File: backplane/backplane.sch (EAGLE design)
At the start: 18 parts, among them J1 09232486825, J2 09232486825, J3 09232486825, J4 09232486825, J5 09232486825, J6 09232486825, J7 09232486825, J8 09232486825, U1 LM1084IS-5.0, U2 LM1084IS-3.3, U3 ESP32-DEVKITC-32D

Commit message: modified backplane
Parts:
- removed C1, C3: 10Uf, rc-master-smd:CP_3216
- removed C2, C4: 10Uf, rc-master-smd:C_1206
- removed JP1: (no value), pinhead:PINHD-1X19
- removed JP2: (no value), pinhead:PINHD-2X15
- removed U1: LM1084IS-5.0, LM1084IS:LM1084IS-5.0
- removed U2: LM1084IS-3.3, LM1084IS:LM1084IS-3.3
- removed U3: ESP32-DEVKITC-32D, ESP32-DEVKITC-32D:ESP32-DEVKITC-32D
- removed XS1: (no value), polyvent_power_connector:CURTIS_INDUSTRIES_T38120-02-0
- added J9: TB009-508-04BE, TB009-508-04BE:TB009-508-04BE
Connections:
- removed net N$1: C3.+, U2.IN
- removed net N$2: C1.+, U1.IN
- removed net N$3: JP1.16, U3.TXD0
- removed net N$4: JP1.15, U3.RXD0
- removed net N$5: JP1.6, U3.IO0
- removed net N$6: JP1.5, U3.IO2
- removed net N$7: JP1.3, U3.SD1
- removed net N$8: JP1.2, U3.SD0
- removed net N$9: JP1.1, U3.CLK
- removed net VCC: U3.EXT_5V
- net 24V/12V: now also J9.2; no longer XS1.P$2
- net 3.3V: now also J1.A7, J1.B7, J2.A7, J2.B7, J3.A7, J3.B7, J4.A7, J4.B7, J5.A7, J5.B7, J6.A7, J6.B7, J7.A7, J7.B7, J8.A7, J8.B7, J9.4; no longer C4.2, J1.C6, J2.C6, J3.C6, J4.C6, J5.C6, J6.C6, J7.C6, J8.C6, JP2.5, U2.OUT, U2.VOUT, U3.3V3
- net 5V: now also J1.C6, J2.C6, J3.C6, J4.C6, J5.C6, J6.C6, J7.C6, J8.C6, J9.3; no longer C2.2, J1.A7, J1.B7, J2.A7, J2.B7, J3.A7, J3.B7, J4.A7, J4.B7, J5.A7, J5.B7, J6.A7, J6.B7, J7.A7, J7.B7, J8.A7, J8.B7, JP2.3, U1.OUT, U1.VOUT
- net EXT_1: no longer JP2.17
- net EXT_2: no longer JP2.19
- net EXT_3: no longer JP2.21
- net EXT_4: no longer JP2.23
- net EXT_5: no longer JP2.25
- net EXT_6: no longer JP2.27
- net EXT_7: no longer JP2.29
- net GND: now also J9.1; no longer C1.-, C2.1, C3.-, C4.1, JP1.13, JP1.19, JP2.1, U1.ADJ/GND, U2.ADJ/GND, U3.GND1, U3.GND2, U3.GND3, XS1.P$1
- net MISO: no longer JP1.12, JP2.9, U3.IO19
- net MOSI: no longer JP1.18, JP2.11, U3.IO23
- net SCK: no longer JP1.11, JP2.7, U3.IO18
- net SCL: no longer JP2.15
- net SDA: no longer JP2.13
- net SS_1: no longer JP1.7, JP2.30, U3.IO4
- net SS_10: no longer JP2.12, U3.IO25
- net SS_11: no longer JP2.10, U3.IO26
- net SS_12: no longer JP2.8, U3.IO32
- net SS_13: no longer JP2.6, U3.IO33
- net SS_14: no longer JP2.4
- net SS_15: no longer JP2.2
- net SS_2: no longer JP1.10, JP2.28, U3.IO5
- net SS_3: no longer JP2.26, U3.IO13
- net SS_4: no longer JP2.24, U3.IO14
- net SS_5: no longer JP1.4, JP2.22, U3.IO15
- net SS_6: no longer JP1.8, JP2.20, U3.IO16
- net SS_7: no longer JP1.9, JP2.18, U3.IO17
- net SS_8: no longer JP1.14, JP2.16, U3.IO21
- net SS_9: no longer JP1.17, JP2.14, U3.IO22

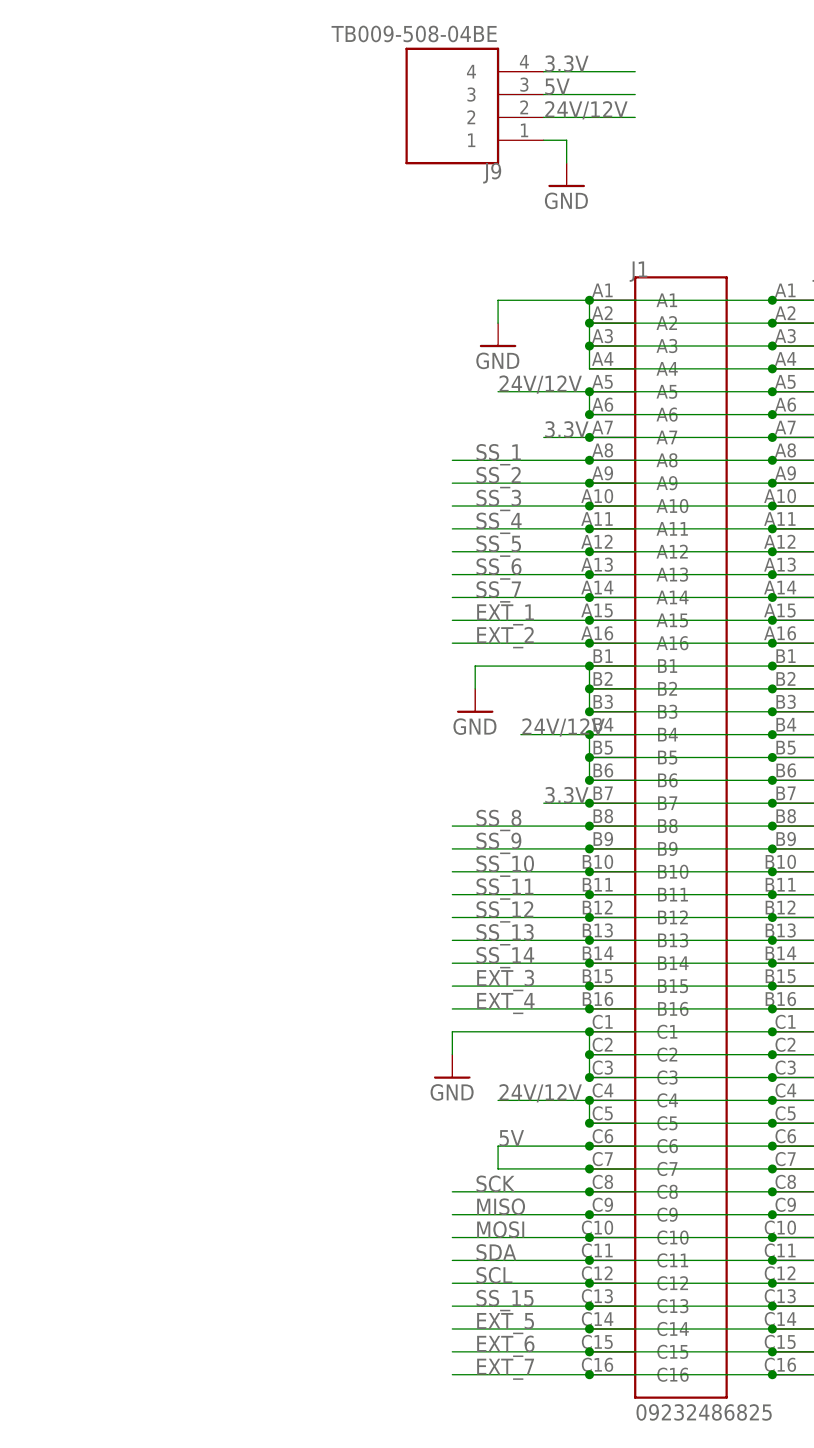
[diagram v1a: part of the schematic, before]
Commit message: added labeled backplane breakout connector, backplane pcb is done
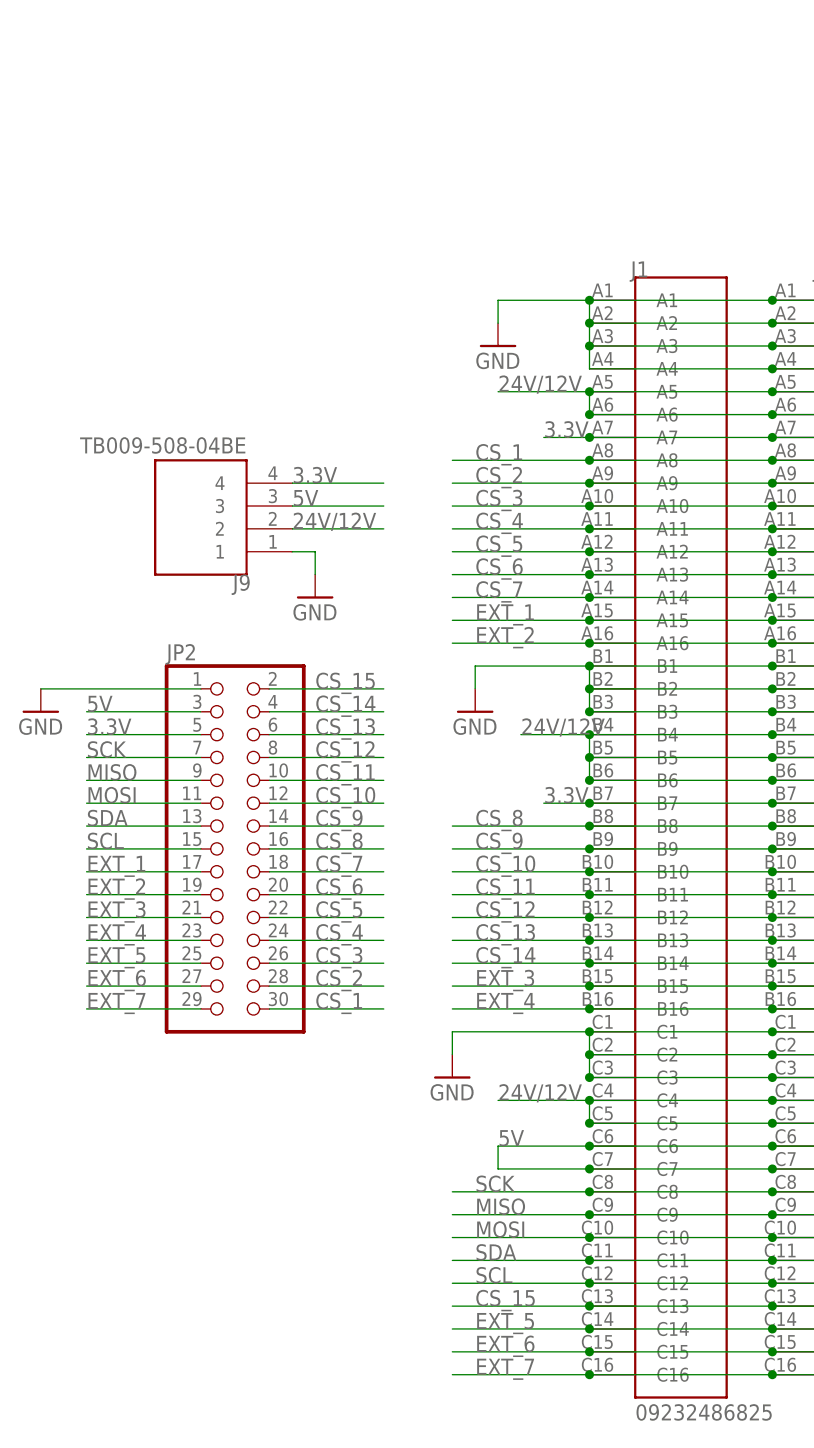
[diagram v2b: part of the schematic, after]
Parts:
- added JP2: (no value), pinhead:PINHD-2X15
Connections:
- removed net SS_1: J1.A8, J2.A8, J3.A8, J4.A8, J5.A8, J6.A8, J7.A8, J8.A8
- removed net SS_10: J1.B10, J2.B10, J3.B10, J4.B10, J5.B10, J6.B10, J7.B10, J8.B10
- removed net SS_11: J1.B11, J2.B11, J3.B11, J4.B11, J5.B11, J6.B11, J7.B11, J8.B11
- removed net SS_12: J1.B12, J2.B12, J3.B12, J4.B12, J5.B12, J6.B12, J7.B12, J8.B12
- removed net SS_13: J1.B13, J2.B13, J3.B13, J4.B13, J5.B13, J6.B13, J7.B13, J8.B13
- removed net SS_14: J1.B14, J2.B14, J3.B14, J4.B14, J5.B14, J6.B14, J7.B14, J8.B14
- removed net SS_15: J1.C13, J2.C13, J3.C13, J4.C13, J5.C13, J6.C13, J7.C13, J8.C13
- removed net SS_2: J1.A9, J2.A9, J3.A9, J4.A9, J5.A9, J6.A9, J7.A9, J8.A9
- removed net SS_3: J1.A10, J2.A10, J3.A10, J4.A10, J5.A10, J6.A10, J7.A10, J8.A10
- removed net SS_4: J1.A11, J2.A11, J3.A11, J4.A11, J5.A11, J6.A11, J7.A11, J8.A11
- removed net SS_5: J1.A12, J2.A12, J3.A12, J4.A12, J5.A12, J6.A12, J7.A12, J8.A12
- removed net SS_6: J1.A13, J2.A13, J3.A13, J4.A13, J5.A13, J6.A13, J7.A13, J8.A13
- removed net SS_7: J1.A14, J2.A14, J3.A14, J4.A14, J5.A14, J6.A14, J7.A14, J8.A14
- removed net SS_8: J1.B8, J2.B8, J3.B8, J4.B8, J5.B8, J6.B8, J7.B8, J8.B8
- removed net SS_9: J1.B9, J2.B9, J3.B9, J4.B9, J5.B9, J6.B9, J7.B9, J8.B9
- new net CS_1: J1.A8, J2.A8, J3.A8, J4.A8, J5.A8, J6.A8, J7.A8, J8.A8, JP2.30
- new net CS_10: J1.B10, J2.B10, J3.B10, J4.B10, J5.B10, J6.B10, J7.B10, J8.B10, JP2.12
- new net CS_11: J1.B11, J2.B11, J3.B11, J4.B11, J5.B11, J6.B11, J7.B11, J8.B11, JP2.10
- new net CS_12: J1.B12, J2.B12, J3.B12, J4.B12, J5.B12, J6.B12, J7.B12, J8.B12, JP2.8
- new net CS_13: J1.B13, J2.B13, J3.B13, J4.B13, J5.B13, J6.B13, J7.B13, J8.B13, JP2.6
- new net CS_14: J1.B14, J2.B14, J3.B14, J4.B14, J5.B14, J6.B14, J7.B14, J8.B14, JP2.4
- new net CS_15: J1.C13, J2.C13, J3.C13, J4.C13, J5.C13, J6.C13, J7.C13, J8.C13, JP2.2
- new net CS_2: J1.A9, J2.A9, J3.A9, J4.A9, J5.A9, J6.A9, J7.A9, J8.A9, JP2.28
- new net CS_3: J1.A10, J2.A10, J3.A10, J4.A10, J5.A10, J6.A10, J7.A10, J8.A10, JP2.26
- new net CS_4: J1.A11, J2.A11, J3.A11, J4.A11, J5.A11, J6.A11, J7.A11, J8.A11, JP2.24
- new net CS_5: J1.A12, J2.A12, J3.A12, J4.A12, J5.A12, J6.A12, J7.A12, J8.A12, JP2.22
- new net CS_6: J1.A13, J2.A13, J3.A13, J4.A13, J5.A13, J6.A13, J7.A13, J8.A13, JP2.20
- new net CS_7: J1.A14, J2.A14, J3.A14, J4.A14, J5.A14, J6.A14, J7.A14, J8.A14, JP2.18
- new net CS_8: J1.B8, J2.B8, J3.B8, J4.B8, J5.B8, J6.B8, J7.B8, J8.B8, JP2.16
- new net CS_9: J1.B9, J2.B9, J3.B9, J4.B9, J5.B9, J6.B9, J7.B9, J8.B9, JP2.14
- net 3.3V: now also JP2.5
- net 5V: now also JP2.3
- net EXT_1: now also JP2.17
- net EXT_2: now also JP2.19
- net EXT_3: now also JP2.21
- net EXT_4: now also JP2.23
- net EXT_5: now also JP2.25
- net EXT_6: now also JP2.27
- net EXT_7: now also JP2.29
- net GND: now also JP2.1
- net MISO: now also JP2.9
- net MOSI: now also JP2.11
- net SCK: now also JP2.7
- net SCL: now also JP2.15
- net SDA: now also JP2.13
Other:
- moved on the sheet: J9

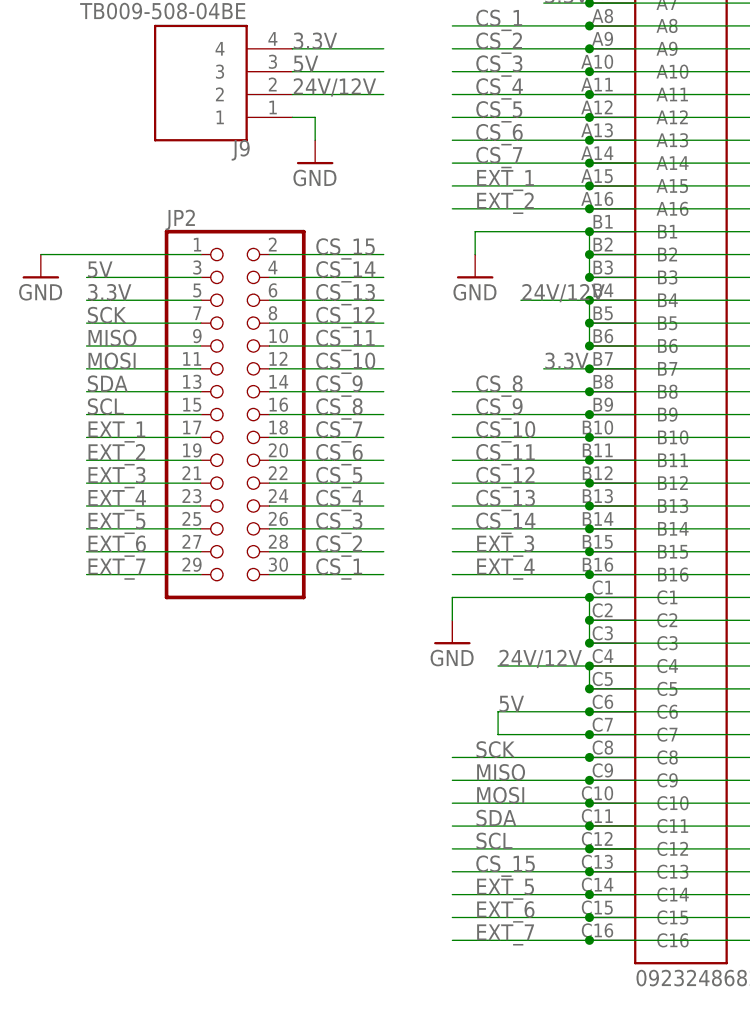
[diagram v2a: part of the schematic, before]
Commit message: added a library for the switch I'll be using, and I updated the backplane pinout
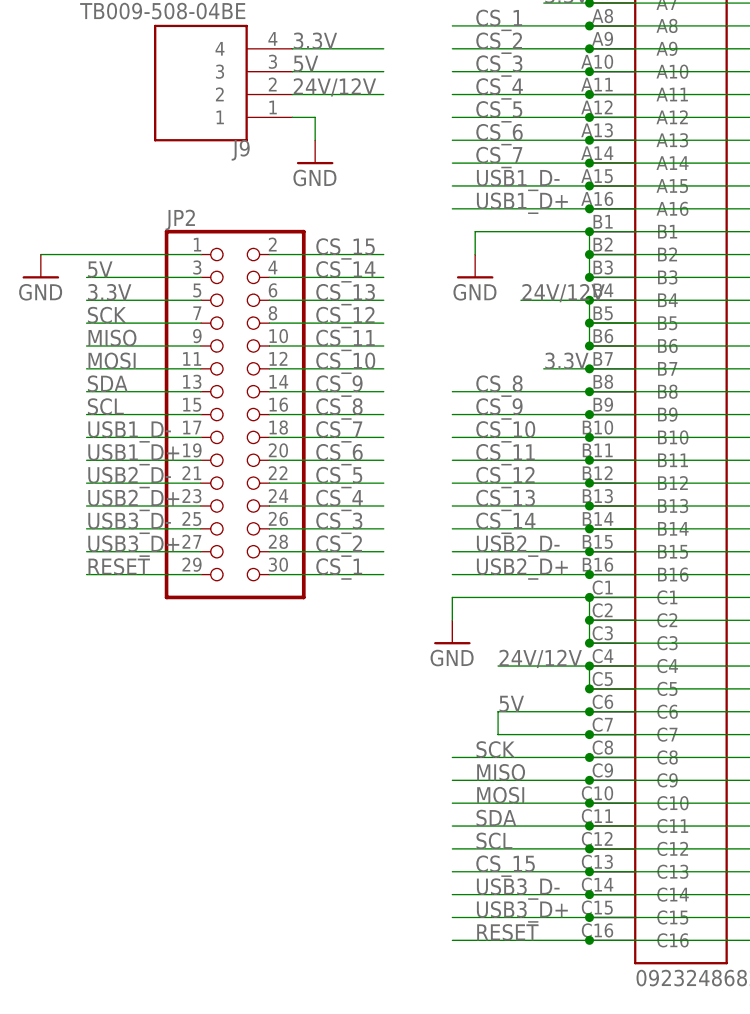
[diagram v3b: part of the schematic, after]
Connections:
- net EXT_1 renamed USB1_D-
- net EXT_2 renamed USB1_D+
- net EXT_3 renamed USB2_D-
- net EXT_4 renamed USB2_D+
- net EXT_5 renamed USB3_D-
- net EXT_6 renamed USB3_D+
- net EXT_7 renamed RESET
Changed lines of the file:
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@@
 </segment>
 </net>
-<net name="EXT_2" class="0">
+<net name="USB1_D+" class="0">
 <segment>
 <pinref part="J8" gate="G$1" pin="A16"/>
@@
 </segment>
 </net>
-<net name="EXT_4" class="0">
+<net name="USB2_D+" class="0">
 <segment>
 <pinref part="J1" gate="G$1" pin="B16"/>
@@
 </segment>
 </net>
-<net name="EXT_5" class="0">
+<net name="USB3_D-" class="0">
 <segment>
 <pinref part="J1" gate="G$1" pin="C14"/>
@@
 </segment>
 </net>
-<net name="EXT_7" class="0">
+<net name="RESET" class="0">
 <segment>
 <pinref part="J1" gate="G$1" pin="C16"/>
@@
 </segment>
 </net>
-<net name="EXT_1" class="0">
+<net name="USB1_D-" class="0">
 <segment>
 <pinref part="J1" gate="G$1" pin="A15"/>
@@
 </segment>
 </net>
-<net name="EXT_3" class="0">
+<net name="USB2_D-" class="0">
 <segment>
 <pinref part="J1" gate="G$1" pin="B15"/>
@@
 </segment>
 </net>
-<net name="EXT_6" class="0">
+<net name="USB3_D+" class="0">
 <segment>
 <pinref part="J1" gate="G$1" pin="C15"/>
